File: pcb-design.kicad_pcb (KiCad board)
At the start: 2 copper layers, 18.8 x 43.7 mm, 13 parts, among them J1 SM04B-SRSS-TBLFSN, J2 SM04B-SRSS-TBLFSN, U2 OS102011MA1QS1, U3 TSIC206-TO92, U4 MOUDLE-SEEEDUINO-XIAO-ESP32C3

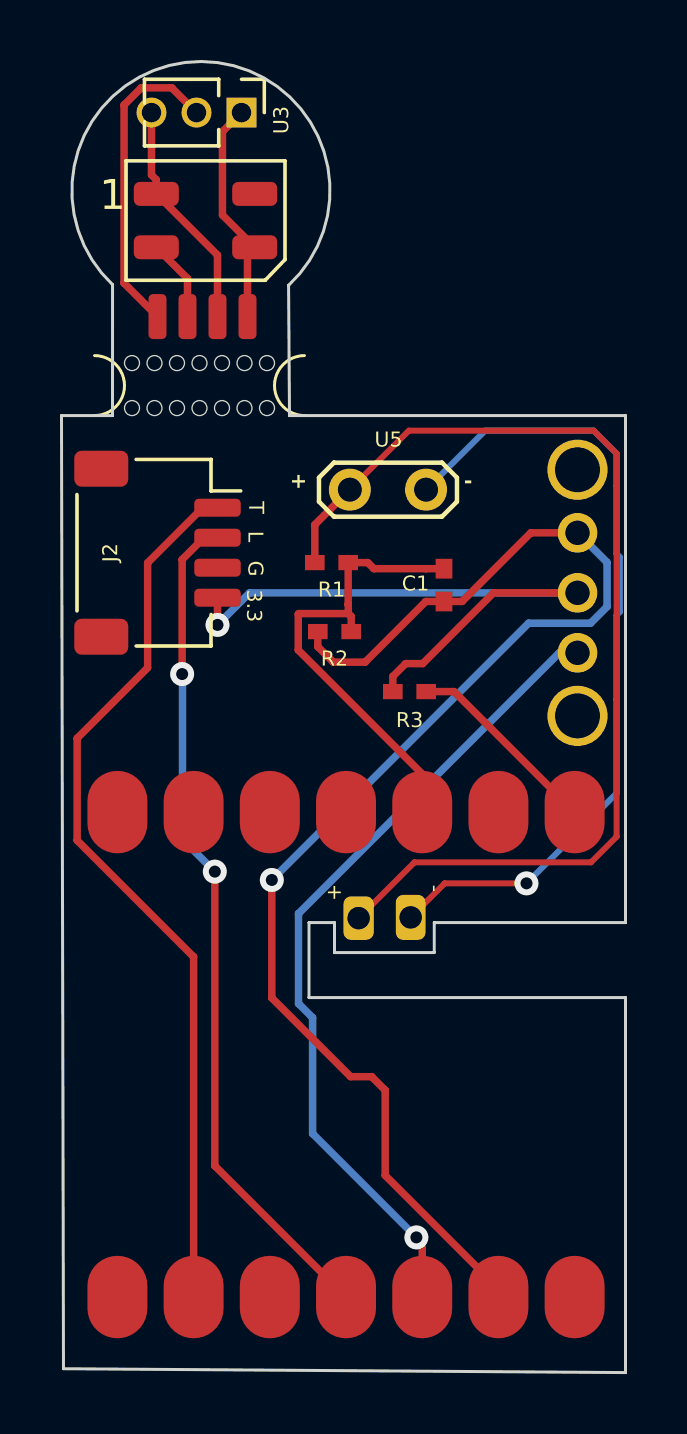
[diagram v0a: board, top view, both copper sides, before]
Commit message: plus ground-header+tempsensor en light differently arranged
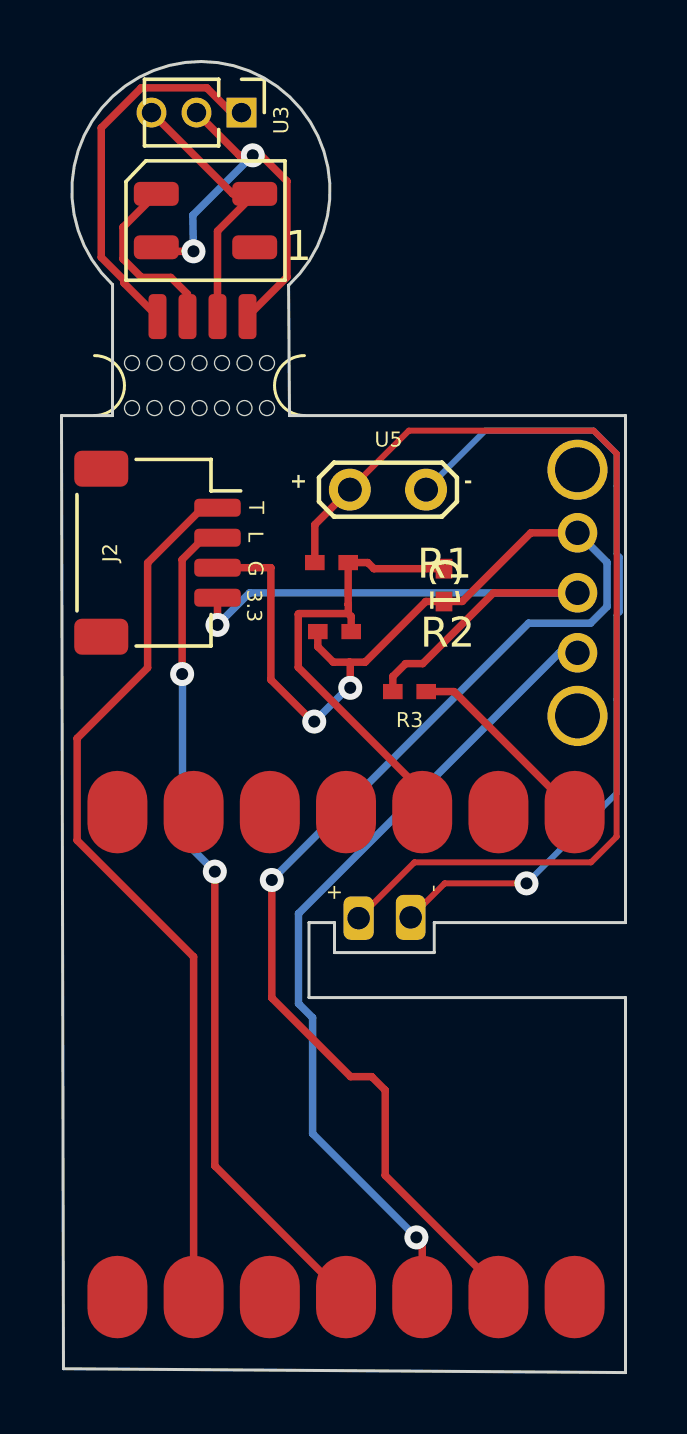
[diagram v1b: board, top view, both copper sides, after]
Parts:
- turned D2 to 180 degrees
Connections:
- D2 pad 1: /GND -> unconnected-(D2-VSS-Pad1)
- D2 pad 2: /Licht -> /G
- D2 pad 3: /3.3v -> /Licht
- D2 pad 4: unconnected-(D2-DOUT-Pad4) -> /3.3V
- J1 pad 3: /GND -> /G
- J1 pad 4: /3.3v -> /3.3V
- J2 pad 3: /G -> /esp-gnd
- U3 pad 1: /3.3v -> /Temp
- U3 pad 2: /Temp -> /3.3V
- U3 pad 3: /GND -> /G
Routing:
- net /3.3V: track 0.00 -> 14.4 mm, vias 0 -> 2
- net /esp-gnd: track 46.4 -> 56.6 mm, vias 1 -> 3
- net /G: track 0.00 -> 9.17 mm
- net /GND: track 7.71 -> 0.00 mm
- net /3.3v: track 7.61 -> 0.00 mm
- net /Licht: track 2.74 -> 6.01 mm
- net /Temp: track 10.5 -> 12.6 mm
